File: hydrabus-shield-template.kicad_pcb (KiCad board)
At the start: 2 copper layers, 60 x 37 mm, 4 parts, among them J1 CONN_02X07, J2 CONN_02X10, J3 CONN_02X10, J4 CONN_01X06

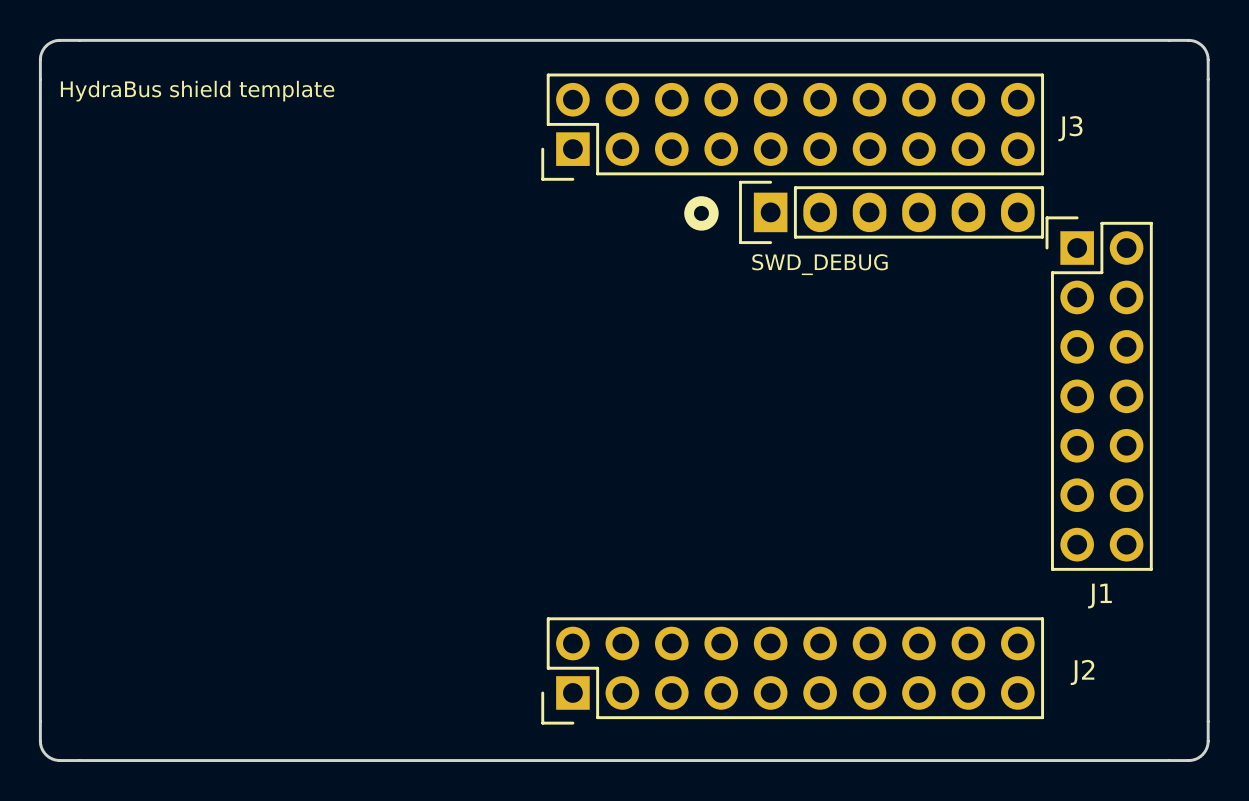
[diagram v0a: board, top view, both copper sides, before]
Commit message: pcb: rotated J1, added silkscreen labels for pins
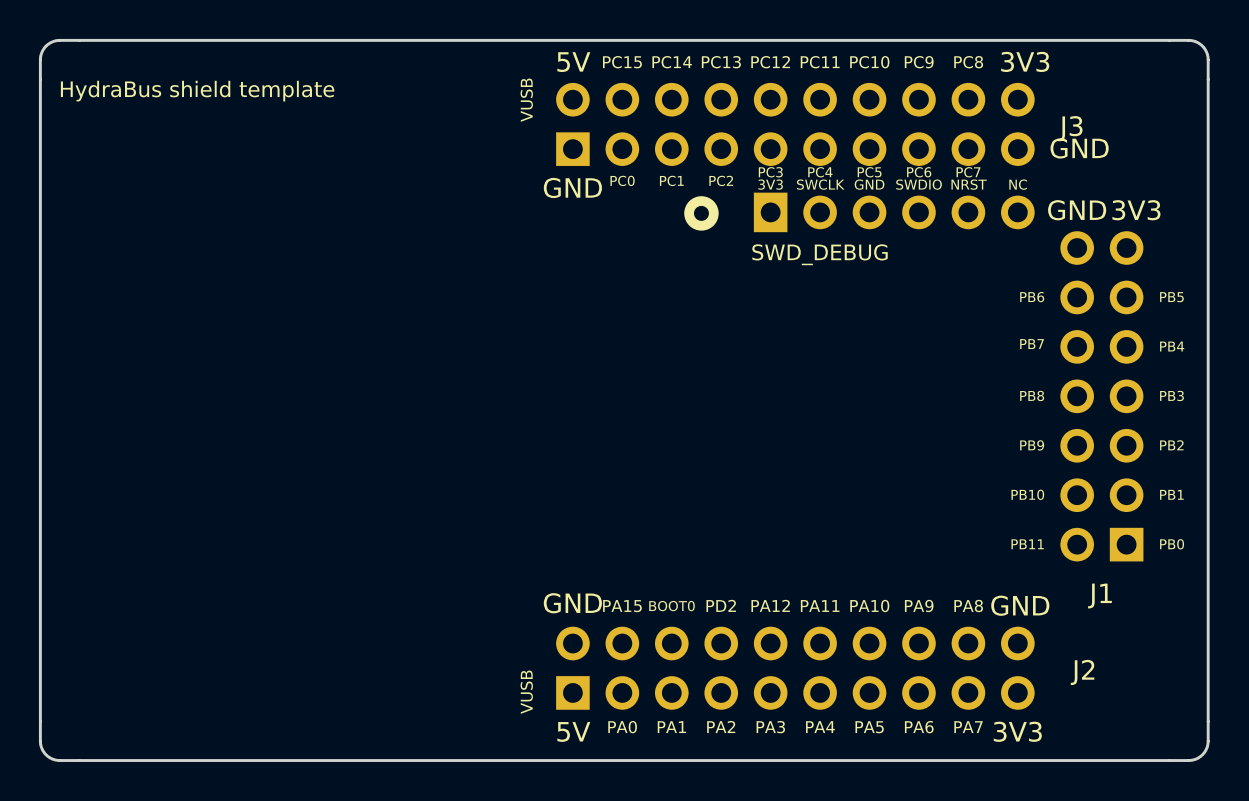
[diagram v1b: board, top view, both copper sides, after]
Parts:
- moved J1 15.5 mm to (171.8, 101.9), turned to 180 degrees
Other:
- board text added: "3V3"
- board text added: "5V"
- board text added: "ADC1_IN0"
- board text added: "ADC2_IN1"
- board text added: "ADC3_IN10"
- board text added: "BOOT0"
- board text added: "DAC1_OUT"
- board text added: "DAC2_OUT"
- board text added: "GND"
- board text added: "I2C1_SCL"
- board text added: "I2C1_SDA"
- board text added: "NC"
- board text added: "NRST"
- board text added: "PA0"
- board text added: "PA1"
- board text added: "PA10"
- board text added: "PA11"
- board text added: "PA12"
- board text added: "PA15"
- board text added: "PA2"
- board text added: "PA3"
- board text added: "PA4"
- board text added: "PA5"
- board text added: "PA6"
- board text added: "PA7"
- board text added: "PA8"
- board text added: "PA9"
- board text added: "PB0"
- board text added: "PB1"
- board text added: "PB10"
- board text added: "PB11"
- board text added: "PB2"
- board text added: "PB3"
- board text added: "PB4"
- board text added: "PB5"
- board text added: "PB6"
- board text added: "PB7"
- board text added: "PB8"
- board text added: "PB9"
- board text added: "PC0"
- board text added: "PC1"
- board text added: "PC10"
- board text added: "PC11"
- board text added: "PC12"
- board text added: "PC13"
- board text added: "PC14"
- board text added: "PC15"
- board text added: "PC2"
- board text added: "PC3"
- board text added: "PC4"
- board text added: "PC5"
- board text added: "PC6"
- board text added: "PC7"
- board text added: "PC8"
- board text added: "PC9"
- board text added: "PD2"
- board text added: "SDIO_CK"
- board text added: "SDIO_CMD"
- board text added: "SDIO_D0"
- board text added: "SDIO_D1"
- board text added: "SDIO_D2"
- board text added: "SDIO_D3"
- board text added: "SPI1_MISO"
- board text added: "SPI1_MOSI"
- board text added: "SPI1_NSS"
- board text added: "SPI1_SCK"
- board text added: "SPI2_MISO"
- board text added: "SPI2_MOSI"
- board text added: "SPI2_SCK"
- board text added: "SWCLK"
- board text added: "SWDIO"
- board text added: "USART1_CK"
- board text added: "USART1_RX"
- board text added: "USART1_TX"
- board text added: "USART2_RX"
- board text added: "USART2_TX"
- board text added: "USB0_D+"
- board text added: "USB0_D-"
- board text added: "VUSB"

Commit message: pcb/sch: updated footprints
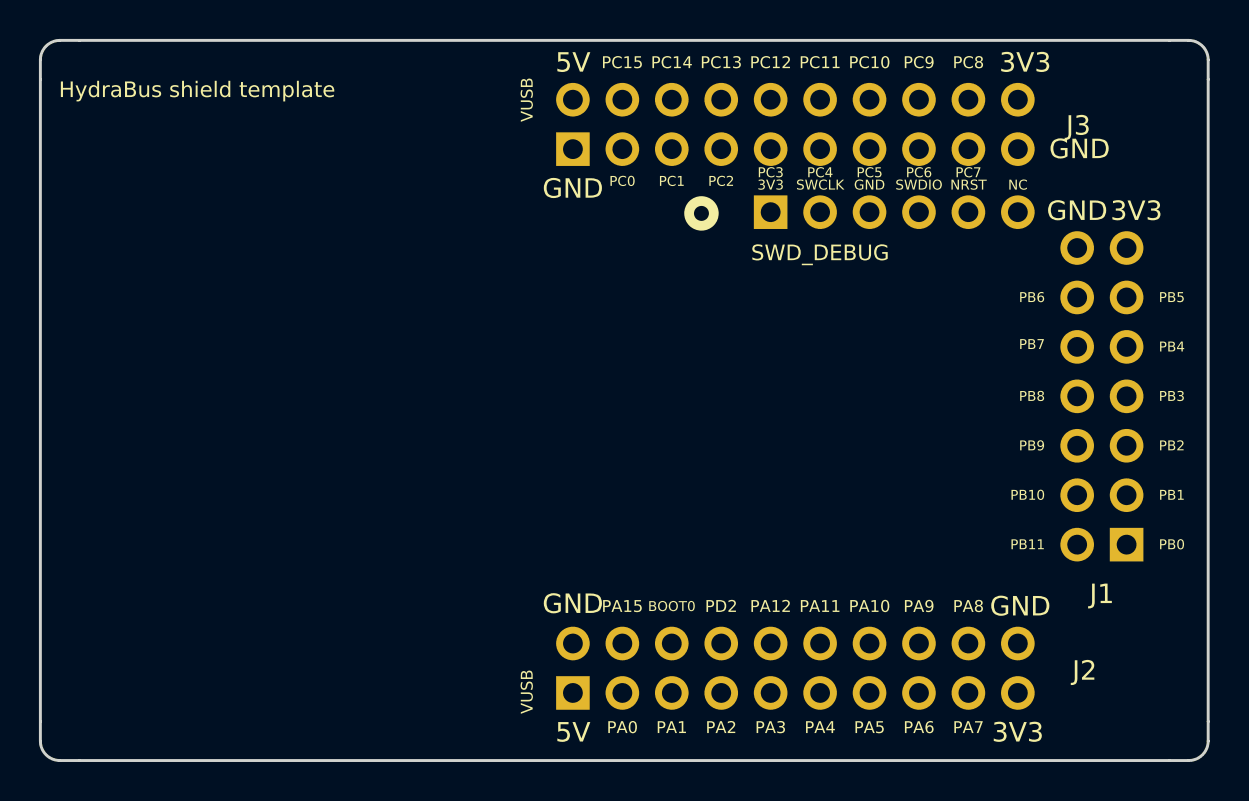
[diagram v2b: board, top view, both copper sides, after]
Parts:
- J1: footprint Pin_Headers:Pin_Header_Straight_2x07 -> umetronics:Hydrabus_Shield_Conn_2x07; moved to B.Cu
- J2, J3: footprint Pin_Headers:Pin_Header_Straight_2x10 -> umetronics:Hydrabus_Shield_Conn_2x10; moved to B.Cu
- J4: footprint Pin_Headers:Pin_Header_Straight_1x06 -> umetronics:Hydrabus_Shield_Conn_1x06; moved to B.Cu
- turned J4 to 0 degrees
- turned J1 to 90 degrees
- turned J2 to 0 degrees
- turned J3 to 0 degrees
